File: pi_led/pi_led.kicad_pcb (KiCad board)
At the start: 2 copper layers, 50 x 50 mm, 13 parts, among them CON1 PWR, P1 LED_STRIP, P2 RiPi, Q1 STP16NF06L, Q2 STP16NF06L, Q3 STP16NF06L

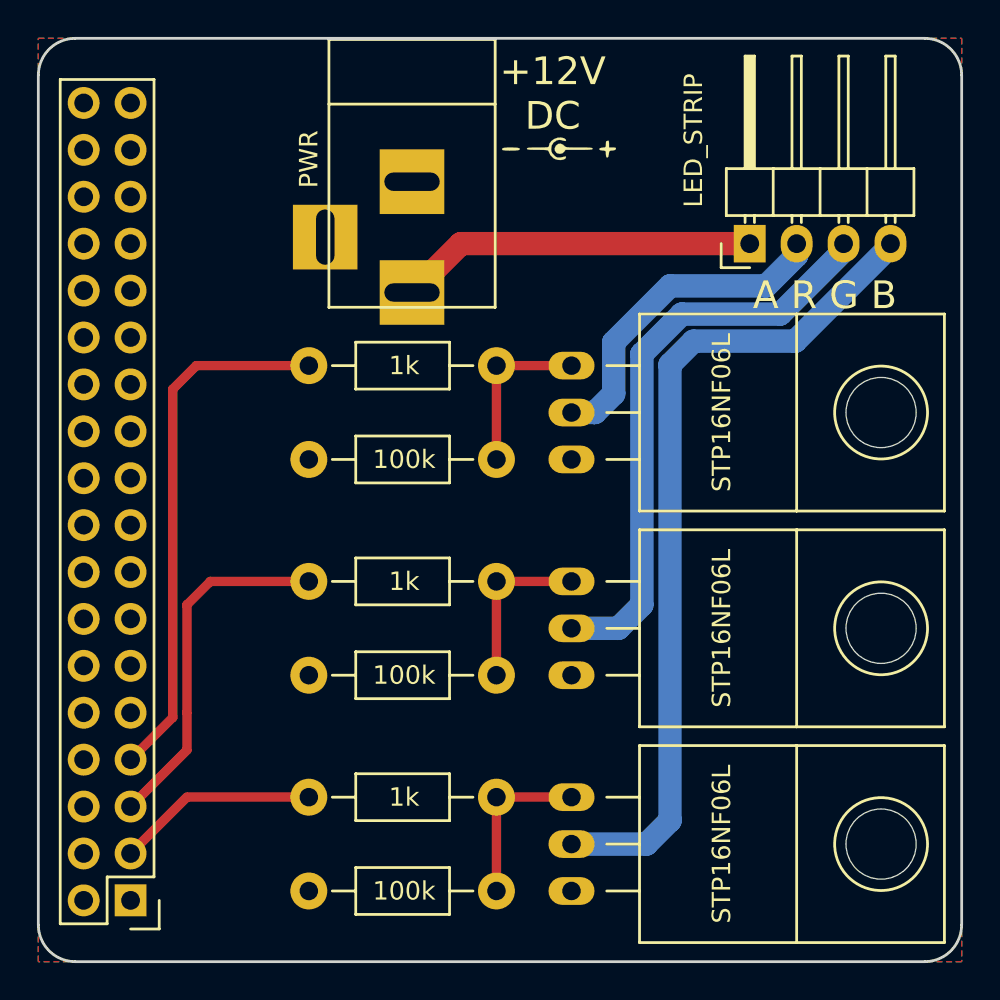
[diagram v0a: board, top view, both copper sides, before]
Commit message: Replaced barrel jack part, no slots
Removed slots from barrel jack part because I don't think Dirty PCBs handles
plated slots nicely.

Tweaked LED_B track because clearance was a little close for comfort

Removed backup file.
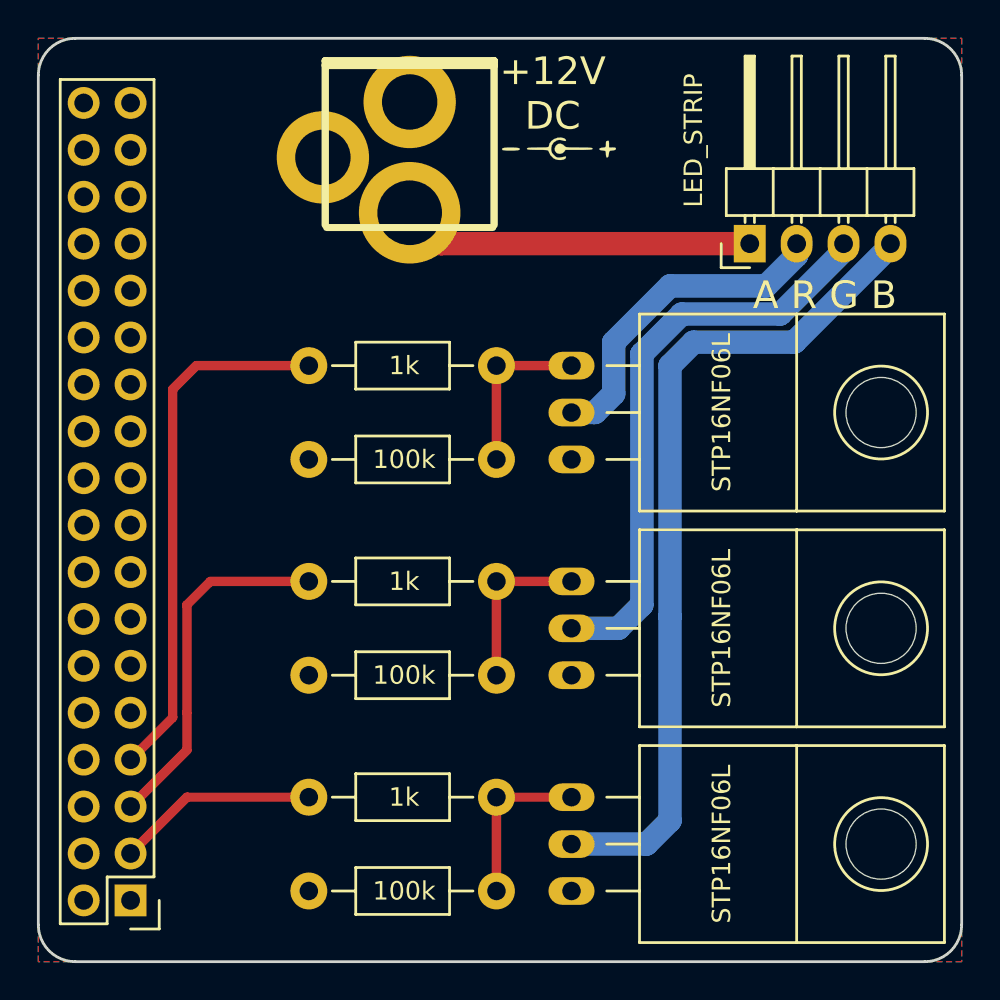
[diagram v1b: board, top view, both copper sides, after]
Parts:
- CON1: footprint Connect:BARREL_JACK -> barrel_jack:barrel_jack
- moved CON1 4.32 mm to (110.1, 63.2)
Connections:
- P2 pad 1: Net-(P2-Pad1) -> (no net)
- P2 pad 10: Net-(P2-Pad10) -> (no net)
- P2 pad 11: Net-(P2-Pad11) -> (no net)
- P2 pad 12: Net-(P2-Pad12) -> (no net)
- P2 pad 13: Net-(P2-Pad13) -> (no net)
- P2 pad 15: Net-(P2-Pad15) -> (no net)
- P2 pad 16: Net-(P2-Pad16) -> (no net)
- P2 pad 17: Net-(P2-Pad17) -> (no net)
- P2 pad 18: Net-(P2-Pad18) -> (no net)
- P2 pad 19: Net-(P2-Pad19) -> (no net)
- P2 pad 2: Net-(P2-Pad2) -> (no net)
- P2 pad 21: Net-(P2-Pad21) -> (no net)
- P2 pad 22: Net-(P2-Pad22) -> (no net)
- P2 pad 23: Net-(P2-Pad23) -> (no net)
- P2 pad 24: Net-(P2-Pad24) -> (no net)
- P2 pad 26: Net-(P2-Pad26) -> (no net)
- P2 pad 27: Net-(P2-Pad27) -> (no net)
- P2 pad 28: Net-(P2-Pad28) -> (no net)
- P2 pad 29: Net-(P2-Pad29) -> (no net)
- P2 pad 31: Net-(P2-Pad31) -> (no net)
- P2 pad 32: Net-(P2-Pad32) -> (no net)
- P2 pad 33: Net-(P2-Pad33) -> (no net)
- P2 pad 35: Net-(P2-Pad35) -> (no net)
- P2 pad 36: Net-(P2-Pad36) -> (no net)
- P2 pad 4: Net-(P2-Pad4) -> (no net)
- P2 pad 8: Net-(P2-Pad8) -> (no net)
